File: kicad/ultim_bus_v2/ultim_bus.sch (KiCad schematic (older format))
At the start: 90 parts, among them M1 MouseBite, M10 MouseBite, M11 MouseBite, M12 MouseBite, M13 MouseBite, M15 MouseBite, M16 MouseBite, M17 MouseBite, M18 MouseBite, M2 MouseBite, M3 MouseBite, M4 MouseBite, M5 MouseBite, M6 MouseBite, M8 MouseBite, M9 MouseBite, P1 CONN_1, P10 CONN_1, P11 CONN_1, P12 CONN_1, P13 CONN_1, P14 CONN_1, P15 CONN_1, P16 CONN_1, P17 CONN_1, P18 CONN_1, P19 CONN_1, P2 CONN_1, P20 CONN_1, P21 CONN_1, P22 CONN_1, P23 CONN_1, P24 CONN_1, P25 CONN_1, P26 CONN_1, P27 CONN_1, P28 CONN_1, P29 CONN_1, P3 CONN_1, P30 CONN_1, P31 CONN_1, P32 CONN_1, P33 CONN_1, P34 CONN_1, P35 CONN_1, P36 CONN_1, P37 CONN_1, P38 CONN_1, P39 CONN_1, P4 CONN_1, P40 CONN_1, P41 CONN_1, P42 CONN_1, P43 CONN_1, P44 CONN_1, P45 CONN_1, P46 CONN_1, P47 CONN_1, P48 CONN_1, P49 CONN_1, P5 CONN_1, P50 CONN_1, P51 CONN_1, P52 CONN_1, P6 CONN_1, P7 CONN_1, P8 CONN_1, P9 CONN_1

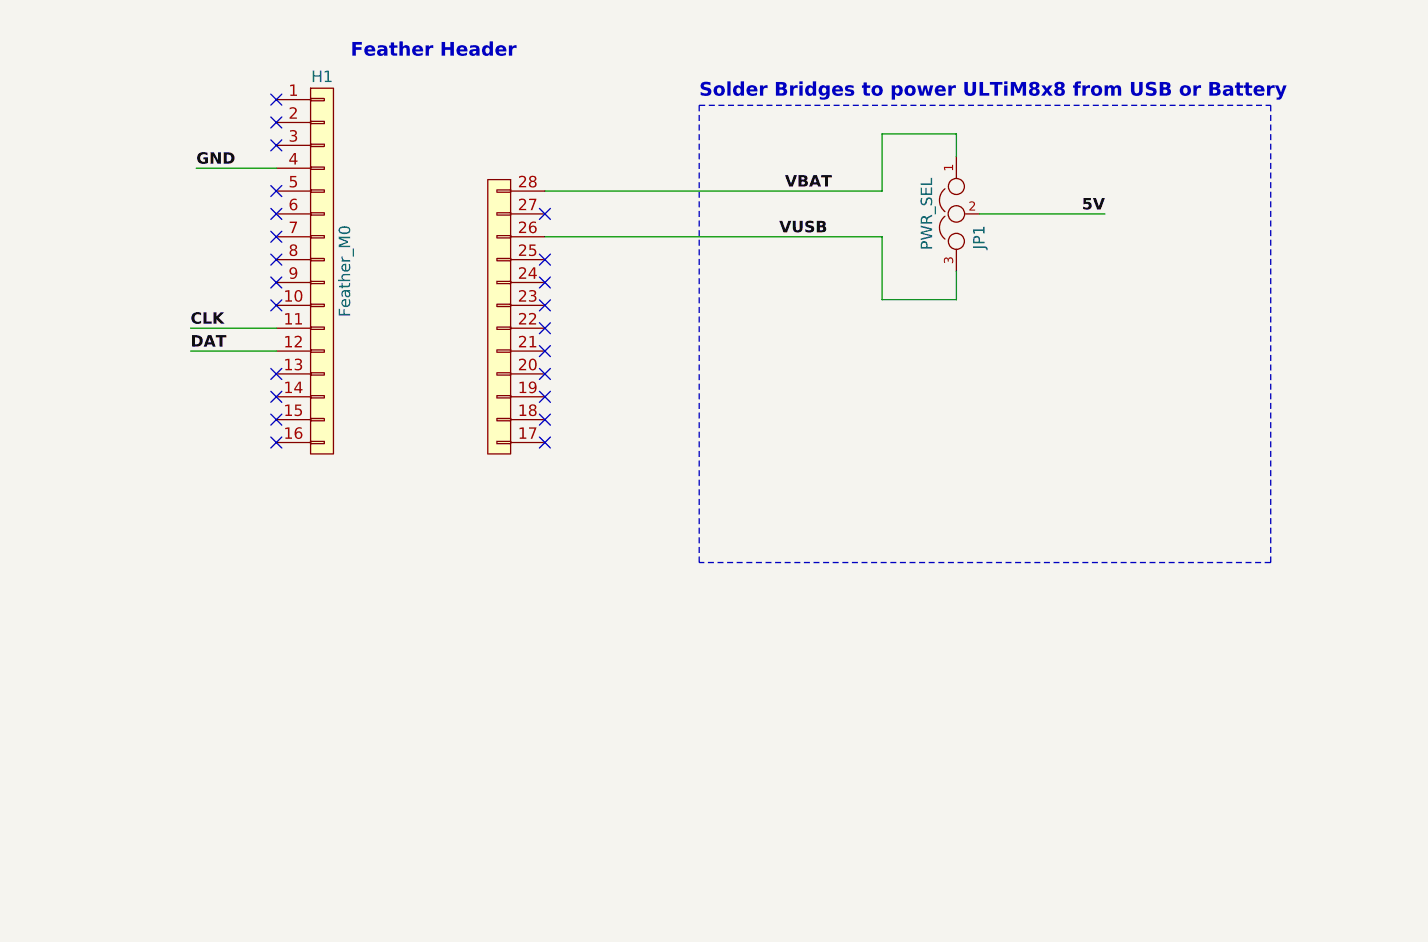
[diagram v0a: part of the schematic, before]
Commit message: added 6 SMD switches to ultim_bus_v2 with pullup resistors
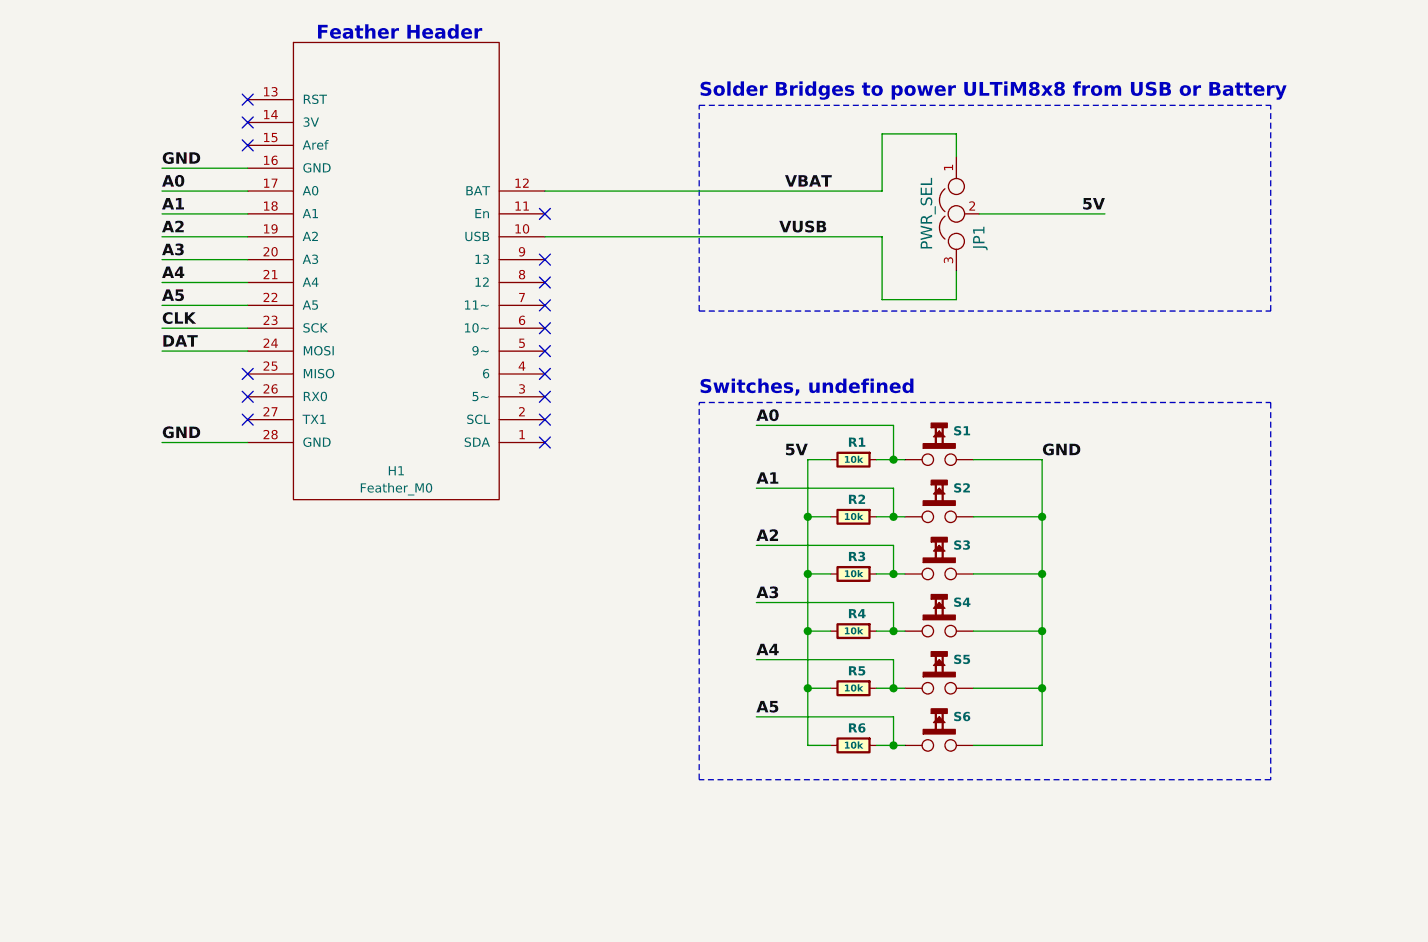
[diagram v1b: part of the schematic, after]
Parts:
- removed H1: Feather_M0, ultim_bus:FEATHER_M0_2, symbol Feather_M0
- added H1: Feather_M0, ultim_bus:FEATHER_M0_2, symbol FeatherM0
- added R1, R2, R3, R4, R5, R6: 10k, ultim_bus:r_0805, symbol R_Small
- added S1, S2, S3, S4, S5, S6: SPST-M-2, ultim_bus:SW_SMD, symbol SPST-M-2
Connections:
- net 5V: now also R1.2, R2.2, R3.2, R4.2, R5.2, R6.2
- net CLK: now also H1.23 (SCK)
- net DAT: now also H1.24 (MOSI)
- net GND: now also H1.16 (GND), H1.28 (GND), S1.2, S2.2, S3.2, S4.2, S5.2, S6.2
- net VBAT: now also H1.12 (BAT)
- net VUSB: now also H1.10 (USB)
- new net A0: H1.17 (A0), R1.1, S1.1
- new net A1: H1.18 (A1), R2.1, S2.1
- new net A2: H1.19 (A2), R3.1, S3.1
- new net A3: H1.20 (A3), R4.1, S4.1
- new net A4: H1.21 (A4), R5.1, S5.1
- new net A5: H1.22 (A5), R6.1, S6.1
- no-connect marks 39 -> 32
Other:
- note added: "Switches, undefined"

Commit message: clean up of all kicad project folders
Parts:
- removed L1, L2: OSHW, ultim_bus:OSHW_6mm, symbol LOGO_1
- removed L11, L12: ULTiM, ultim_bus:logo_ultim8x8_small, symbol LOGO_1
- removed L3, L4: WyoLum, ultim_bus:logo_wyo_butterfly_small, symbol LOGO_1
- removed L7, L8: Maniacal, ultim_bus:logo_MLlabs_small, symbol LOGO_1
- added L1, L2: OSHW, ultim_bus:OSHW_6mm, symbol OSHW
- added L11, L12: LOGO_U88, ultim_bus:logo_ultim8x8_small, symbol LOGO_U88
- added L3, L4: LOGO_WL, ultim_bus:logo_wyo_butterfly_small, symbol LOGO_WL
- added L7, L8: LOGO_ML, ultim_bus:logo_MLlabs_small, symbol LOGO_ML
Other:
- moved on the sheet: v1, v10, v11, v12, v2, v3, v4, v5, v6, v7, v8, v9
